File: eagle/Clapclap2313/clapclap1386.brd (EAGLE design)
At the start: 50 x 50 mm, 26 parts, among them IC1 TINY13-20PU, J1 AVR_SPI_PRG_6PTH, K1 4052, M1 Mic, U1 LM386

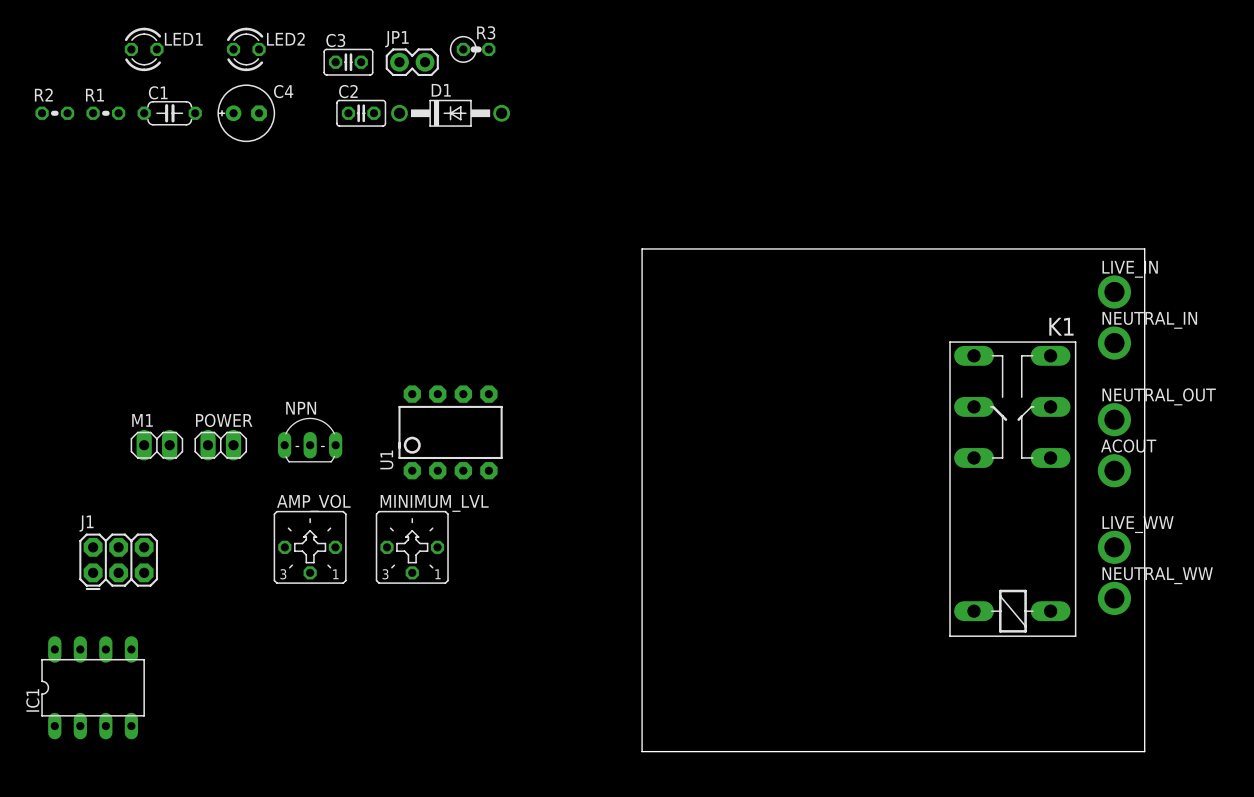
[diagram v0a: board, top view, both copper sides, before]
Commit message: Clapclap 1386 Beta version : needs holes and full verification
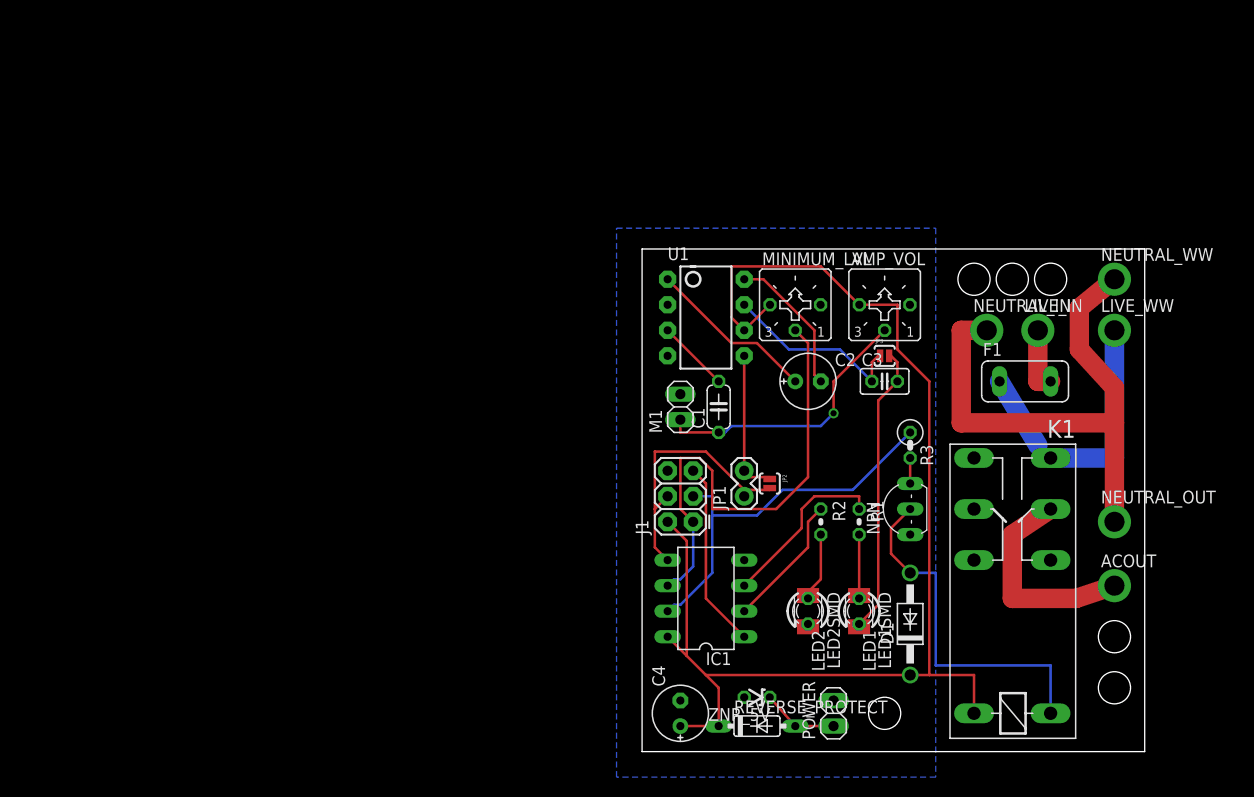
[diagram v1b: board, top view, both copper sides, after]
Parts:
- added F1: (no value), fuse:TE5
- added JP2, JP3: (no value), SparkFun-Passives:SJ_2S-NO
- added LED1SMD: red, led:KA-3528ASYC
- added LED2SMD: green, led:KA-3528ASYC
- added REVERSE_PROTECT: 1N4148DO35-7, diode:DO35-7
- added ZNR_5V: 5V, diode:ZDIO-2.5
- C2: value 1uF -> 10uF; device resistor:C025-025X050 -> resistor:E2,5-6E
- C3: value (none) -> >0.1uF
- moved LED1 90.4 mm to (21.6, 14.0), turned to 270 degrees
- moved R2 86.4 mm to (17.8, 22.9), turned to 270 degrees
- moved R1 85.2 mm to (21.6, 22.9), turned to 270 degrees
- moved LED2 79.0 mm to (16.5, 14.0), turned to 270 degrees
- moved C4 73.7 mm to (3.81, 3.81), turned to 90 degrees
- moved D1 68.3 mm to (26.7, 12.7), turned to 90 degrees
- moved POWER 66.5 mm to (19.1, 3.81), turned to 90 degrees
- moved C3 62.1 mm to (24.1, 36.8)
- moved AMP_VOL 62.0 mm to (24.1, 44.5)
- moved C1 61.9 mm to (7.62, 34.3), turned to 90 degrees
- moved IC1 61.6 mm to (6.35, 15.2), turned to 90 degrees
- moved NPN 60.0 mm to (26.7, 24.1), turned to 90 degrees
- moved J1 59.9 mm to (5.08, 22.9), turned to 90 degrees
- moved R3 58.4 mm to (26.7, 30.5), turned to 270 degrees
- moved JP1 55.1 mm to (10.2, 25.4), turned to 90 degrees
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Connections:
- new net N$18: POWER.1, REVERSE_PROTECT.A, ZNR_5V.C
- new net N$19: F1.2, LIVE_IN.1
- net ACIN: now also F1.1; no longer LIVE_IN.1
- net GND: now also JP3.2, LED1SMD.C, LED2SMD.C, ZNR_5V.A
- net N$10: now also JP2.2
- net N$11: now also LED2SMD.A
- net N$14: now also C2.-; no longer C2.2
- net N$15: now also JP3.1
- net N$17: now also JP2.1
- net N$5: now also C2.+; no longer C2.1
- net N$7: now also LED1SMD.A
- net VCC: now also REVERSE_PROTECT.C; no longer POWER.1
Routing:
- net VCC: track 0.00 -> 126.1 mm
- net N$13: track 0.00 -> 54.1 mm
- net N$12: track 0.00 -> 48.1 mm
- net N$2: track 0.00 -> 38.7 mm
- net N$9: track 0.00 -> 35.9 mm
- net GND: track 0.00 -> 29.3 mm
- net ACIN: track 0.00 -> 28.3 mm
- net N$3: track 0.00 -> 27.7 mm, vias 0 -> 1
- net N$10: track 0.00 -> 26.9 mm
- net ACOUT: track 0.00 -> 21.3 mm
- net N$15: track 0.00 -> 18.8 mm
- net N$16: track 0.00 -> 18.6 mm
- net N$6: track 0.00 -> 17.5 mm
- net N$5: track 0.00 -> 16.9 mm
- net N$17: track 0.00 -> 14.8 mm
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- added copper zone on layer 16, net GND

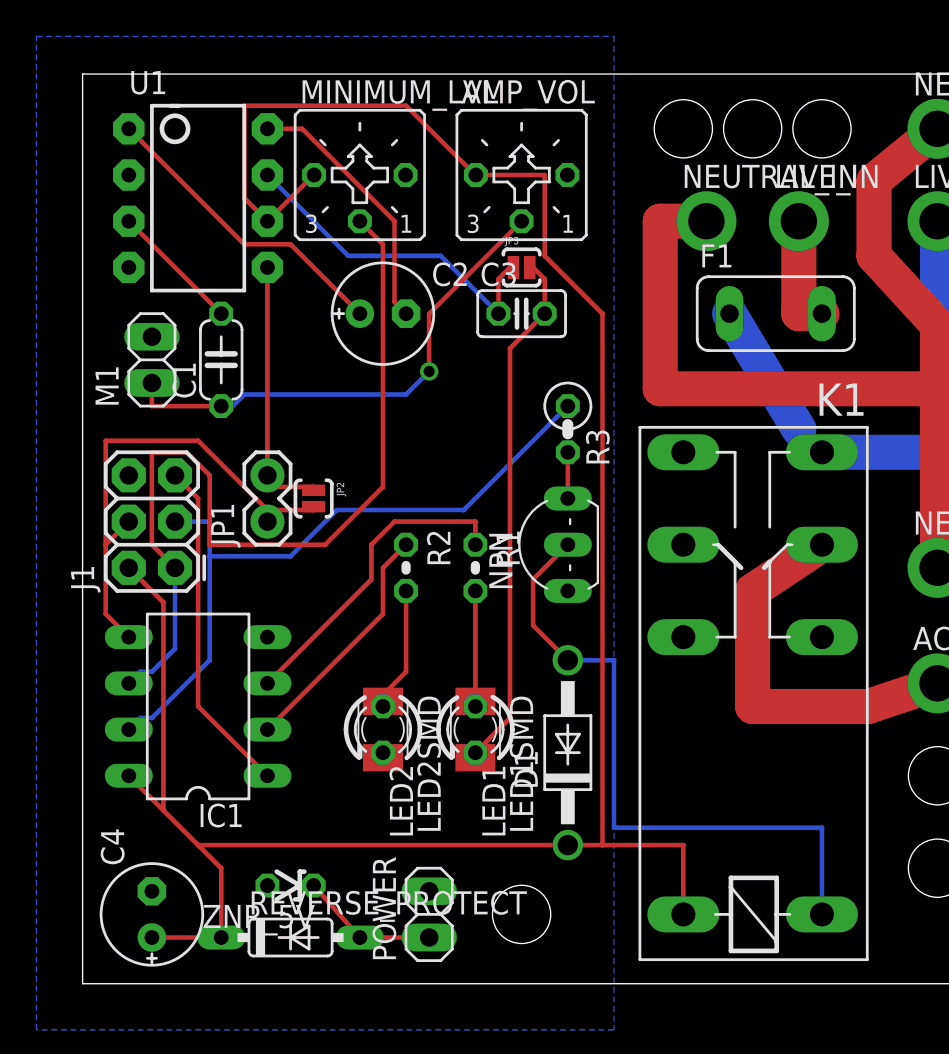
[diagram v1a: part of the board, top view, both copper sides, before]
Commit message: clapclap1386.brd : placement of components ok, must do the silk screen.
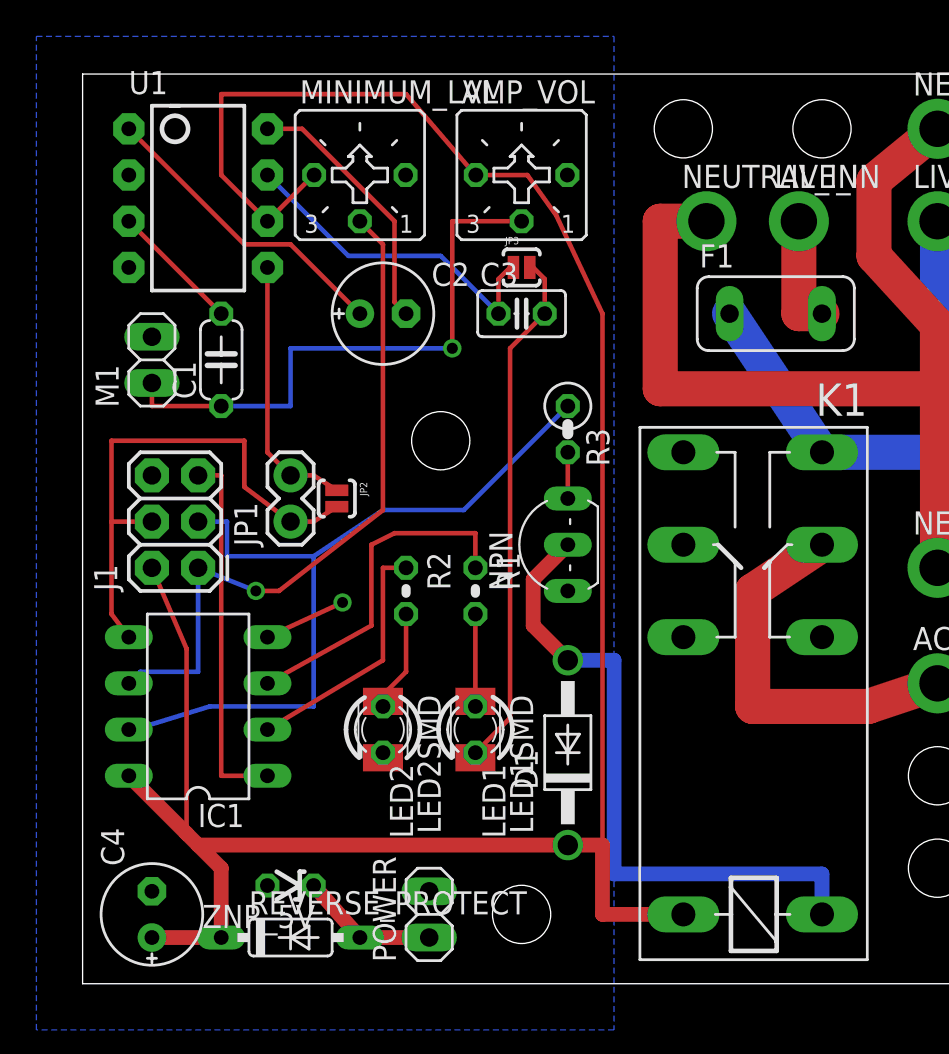
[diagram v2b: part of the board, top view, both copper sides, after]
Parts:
- moved JP2 1.27 mm to (14.0, 26.7)
- moved J1 1.27 mm to (6.35, 22.9)
- moved JP1 1.27 mm to (11.4, 25.4)
- moved R1 1.27 mm to (21.6, 21.6)
- moved R2 1.27 mm to (17.8, 21.6)
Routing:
- net N$12: track 48.1 -> 38.1 mm, vias 0 -> 1
- net N$2: track 38.7 -> 44.3 mm
- net GND: track 29.3 -> 33.8 mm, vias 0 -> 1
- net N$3: track 27.7 -> 31.7 mm
- net VCC: track 126.1 -> 128.7 mm
- net N$10: track 26.9 -> 29.1 mm
- net N$16: track 18.6 -> 20.3 mm
- net N$7: track 6.63 -> 5.36 mm
- net N$11: track 7.16 -> 5.89 mm
- net N$6: track 17.5 -> 18.8 mm
